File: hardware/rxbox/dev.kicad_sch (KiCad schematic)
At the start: 1 part

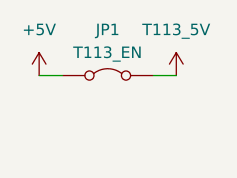
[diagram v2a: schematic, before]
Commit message: wiring wifi + bt to t113
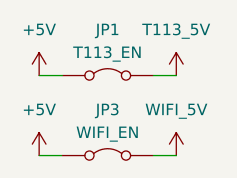
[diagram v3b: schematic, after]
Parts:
- added JP3: WIFI_EN, symbol Jumper:Jumper_2_Bridged
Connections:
- net +5V: now also JP3.1 (A)
- new net WIFI_5V: JP3.2 (B)
